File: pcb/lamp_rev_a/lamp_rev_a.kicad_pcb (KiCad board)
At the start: 4 copper layers, 100 x 80 mm, 107 parts, among them J1 TYPE-C 3.1 MT 16P, J2 DC-005-5A-2.0, J3 DB128H-5.08-2P-BK-S, Q1 AO3400A, Q2 MMBT3904, Q3 MMBT3904, Q4 MMBT3904, Q5 MMBT3904, Q6 MMBT3904, Q7 MMBT3904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

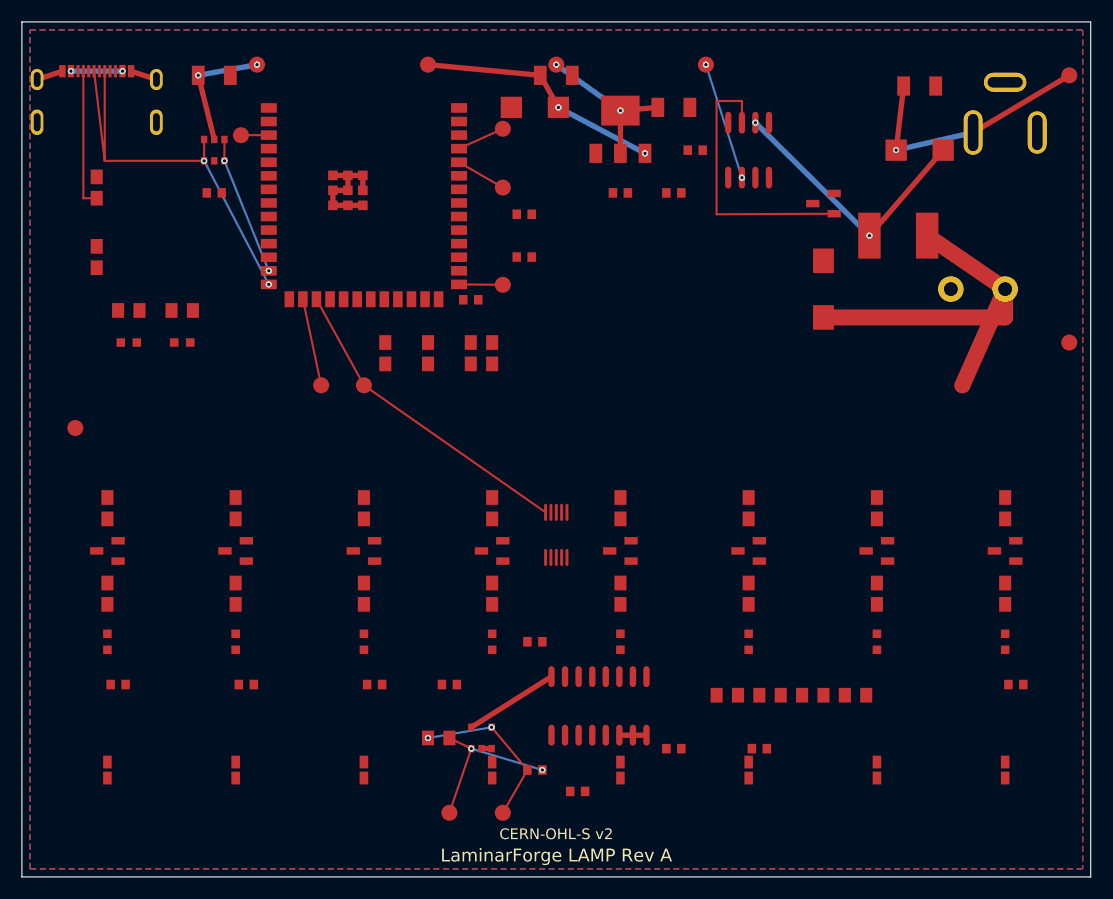
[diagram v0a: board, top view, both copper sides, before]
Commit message: Advance LAMP Rev A routed board seed
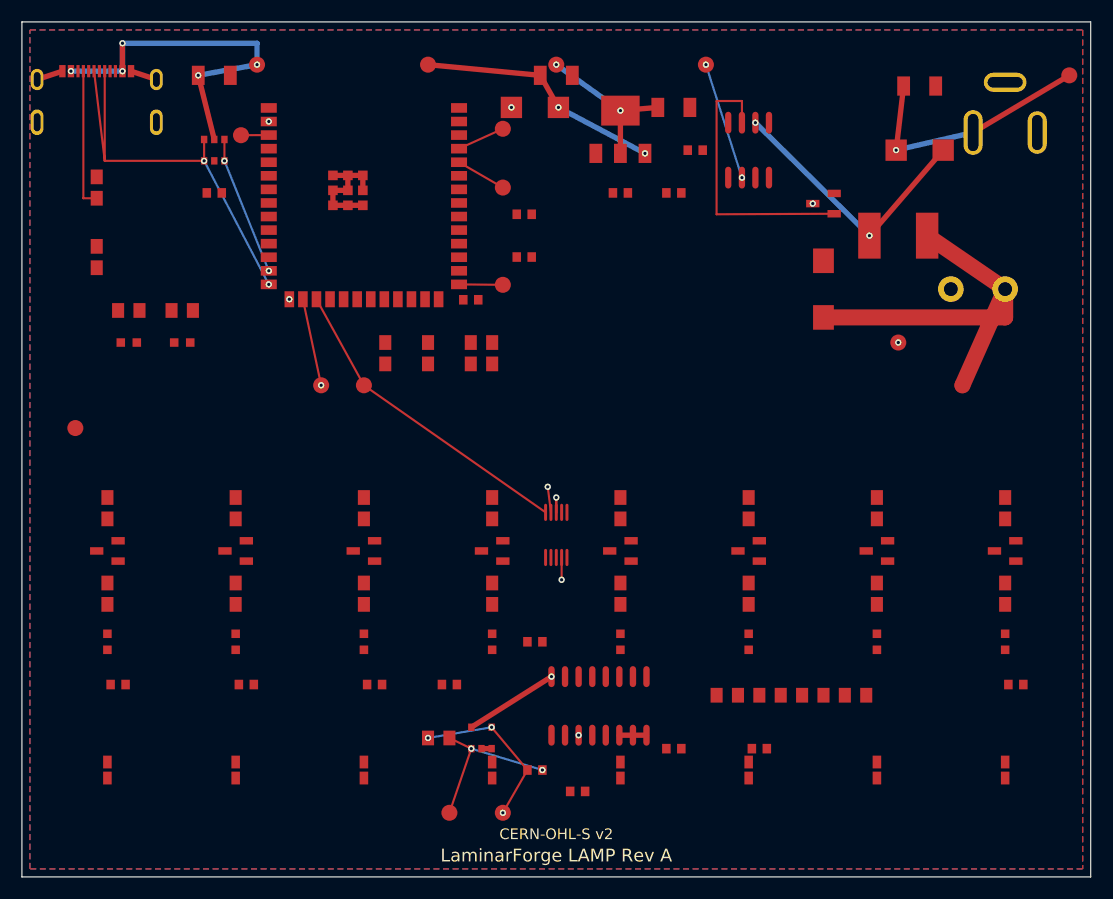
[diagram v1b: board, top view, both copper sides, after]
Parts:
- moved TP_HEATER 16.0 mm to (82.0, 30.0)
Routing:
- net +3V3: track 23.8 -> 118.4 mm, vias 2 -> 5
- net HEATER_PWM: track 11.1 -> 76.9 mm, vias 2 -> 3
- net VBUS: track 16.6 -> 60.5 mm, vias 4 -> 6
- net SDA: track 8.23 -> 41.3 mm, vias 0 -> 2
- net HEATER_P: track 0.00 -> 27.9 mm, vias 0 -> 2
- net ADC_AIN1: track 15.6 -> 41.9 mm, vias 2 -> 3
- net MUX_COM: track 15.9 -> 30.2 mm, vias 2 -> 4

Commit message: Route LAMP Rev A mux bus
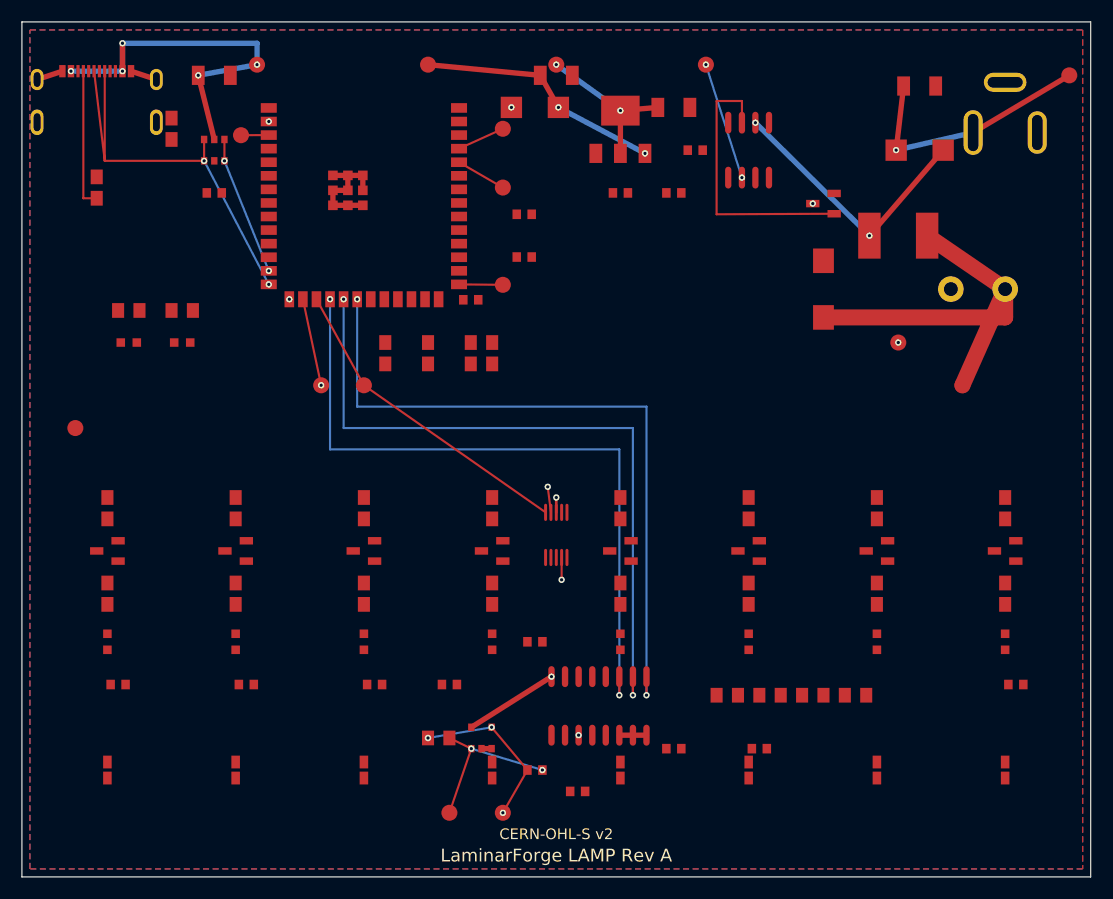
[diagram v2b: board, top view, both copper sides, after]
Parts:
- moved R2 13.9 mm to (14.0, 10.0)
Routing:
- net MUX_S2: track 0.00 -> 65.9 mm, vias 0 -> 2
- net MUX_S1: track 0.00 -> 65.9 mm, vias 0 -> 2
- net MUX_S0: track 0.00 -> 65.9 mm, vias 0 -> 2
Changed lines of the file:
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@@
   	(generator_version "10.0")
   	(layer "F.Cu")
-  	(at 7 22 90)
+  	(at 14 10 90)
   	(property "Reference" "R2"
   		(at 0 -4 0)
@@
   )
   (via
+    (at 28.830 25.950)
+    (size 0.6)
+    (drill 0.3)
+    (layers "F.Cu" "B.Cu")
+    (net 15)
+  )
+  (segment
+    (start 28.830 25.950)
+    (end 28.830 40)
+    (width 0.200)
+    (layer "B.Cu")
+    (net 15)
+  )
+  (segment
+    (start 28.830 40)
+    (end 55.900 40)
+    (width 0.200)
+    (layer "B.Cu")
+    (net 15)
+  )
+  (via
+    (at 55.900 63)
+    (size 0.6)
+    (drill 0.3)
+    (layers "F.Cu" "B.Cu")
+    (net 15)
+  )
+  (segment
+    (start 55.900 40)
+    (end 55.900 63)
+    (width 0.200)
+    (layer "B.Cu")
+    (net 15)
+  )
+  (segment
+    (start 55.900 63)
+    (end 55.900 61.260)
+    (width 0.200)
+    (layer "F.Cu")
+    (net 15)
+  )
+  (via
+    (at 30.100 25.950)
+    (size 0.6)
+    (drill 0.3)
+    (layers "F.Cu" "B.Cu")
+    (net 16)
+  )
+  (segment
+    (start 30.100 25.950)
+    (end 30.100 38)
+    (width 0.200)
+    (layer "B.Cu")
+    (net 16)
+  )
+  (segment
+    (start 30.100 38)
+    (end 57.170 38)
+    (width 0.200)
+    (layer "B.Cu")
+    (net 16)
+  )
+  (via
+    (at 57.170 63)
+    (size 0.6)
+    (drill 0.3)
+    (layers "F.Cu" "B.Cu")
+    (net 16)
+  )
+  (segment
+    (start 57.170 38)
+    (end 57.170 63)
+    (width 0.200)
+    (layer "B.Cu")
+    (net 16)
+  )
+  (segment
+    (start 57.170 63)
+    (end 57.170 61.260)
+    (width 0.200)
+    (layer "F.Cu")
+    (net 16)
+  )
+  (via
+    (at 31.370 25.950)
+    (size 0.6)
+    (drill 0.3)
+    (layers "F.Cu" "B.Cu")
+    (net 17)
+  )
+  (segment
+    (start 31.370 25.950)
+    (end 31.370 36)
+    (width 0.200)
+    (layer "B.Cu")
+    (net 17)
+  )
+  (segment
+    (start 31.370 36)
+    (end 58.440 36)
+    (width 0.200)
+    (layer "B.Cu")
+    (net 17)
+  )
+  (via
+    (at 58.440 63)
+    (size 0.6)
+    (drill 0.3)
+    (layers "F.Cu" "B.Cu")
+    (net 17)
+  )
+  (segment
+    (start 58.440 36)
+    (end 58.440 63)
+    (width 0.200)
+    (layer "B.Cu")
+    (net 17)
+  )
+  (segment
+    (start 58.440 63)
+    (end 58.440 61.260)
+    (width 0.200)
+    (layer "F.Cu")
+    (net 17)
+  )
+  (via

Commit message: Complete LAMP Rev A routed board seed
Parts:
- moved TP_EN 5.00 mm to (25.5, 10.6)
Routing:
- net USB_DN: track 13.1 -> 46.7 mm
- net USB_CC2: track 0.00 -> 21.1 mm
- net GND: track 19.7 -> 20.7 mm, vias 0 -> 2
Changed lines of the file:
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@@
   (footprint "lcsc:TESTPOINT_SMD_1.5MM"
     (layer "F.Cu")
-    (at 20.500 10.600 0)
+    (at 25.500 10.600 0)
     (property "Reference" "TP_EN" (at 0 -1.8 0) (layer "F.Fab") (effects (font (size 0.8 0.8) (thickness 0.1))))
     (property "Value" "ESP_EN" (at 0 1.8 0) (layer "F.Fab") (effects (font (size 0.8 0.8) (thickness 0.1))))
@@
   )
   (segment
-    (start 20.500 10.600)
+    (start 25.500 10.600)
     (end 23.100 10.590)
     (width 0.200)
@@
   )
   (via
+    (at 1.500 1.500)
+    (size 0.6)
+    (drill 0.3)
+    (layers "F.Cu" "B.Cu")
+    (net 1)
+  )
+  (via
+    (at 2.500 1.500)
+    (size 0.6)
+    (drill 0.3)
+    (layers "F.Cu" "B.Cu")
+    (net 1)
+  )
+  (segment
+    (start 1.500 1.500)
+    (end 2.500 1.500)
+    (width 0.500)
+    (layer "B.Cu")
+    (net 1)
+  )
+  (segment
+    (start 6.250 4.610)
+    (end 6.250 0.800)
+    (width 0.200)
+    (layer "F.Cu")
+    (net 19)
+  )
+  (segment
+    (start 7.250 4.610)
+    (end 7.250 0.800)
+    (width 0.200)
+    (layer "F.Cu")
+    (net 19)
+  )
+  (segment
+    (start 6.250 0.800)
+    (end 7.250 0.800)
+    (width 0.200)
+    (layer "F.Cu")
+    (net 19)
+  )
+  (segment
+    (start 7.250 0.800)
+    (end 20.500 0.800)
+    (width 0.200)
+    (layer "F.Cu")
+    (net 19)
+  )
+  (segment
+    (start 20.500 0.800)
+    (end 20.500 11)
+    (width 0.200)
+    (layer "F.Cu")
+    (net 19)
+  )
+  (segment
+    (start 20.500 11)
+    (end 18.950 11)
+    (width 0.200)
+    (layer "F.Cu")
+    (net 19)
+  )
+  (segment
+    (start 8.750 4.610)
+    (end 8.750 1.400)
+    (width 0.200)
+    (layer "F.Cu")
+    (net 21)
+  )
+  (segment
+    (start 8.750 1.400)
+    (end 15.500 1.400)
+    (width 0.200)
+    (layer "F.Cu")
+    (net 21)
+  )
+  (segment
+    (start 15.500 1.400)
+    (end 15.500 11)
+    (width 0.200)
+    (layer "F.Cu")
+    (net 21)
+  )
+  (segment
+    (start 15.500 11)
+    (end 14 11)
+    (width 0.200)
+    (layer "F.Cu")
+    (net 21)
+  )
+  (via
     (at 28.830 25.950)
     (size 0.6)
@@
     (connect_pads yes (clearance 0.200))
     (min_thickness 0.150)
-    (fill yes (thermal_gap 0.300) (thermal_bridge_width 0.300))
+    (fill yes (thermal_gap 0.300) (thermal_bridge_width 0.300) (island_removal_mode 0))
     (polygon
       (pts
@@
     (connect_pads yes (clearance 0.200))
     (min_thickness 0.150)
-    (fill yes (thermal_gap 0.300) (thermal_bridge_width 0.300))
+    (fill yes (thermal_gap 0.300) (thermal_bridge_width 0.300) (island_removal_mode 0))
     (polygon
       (pts

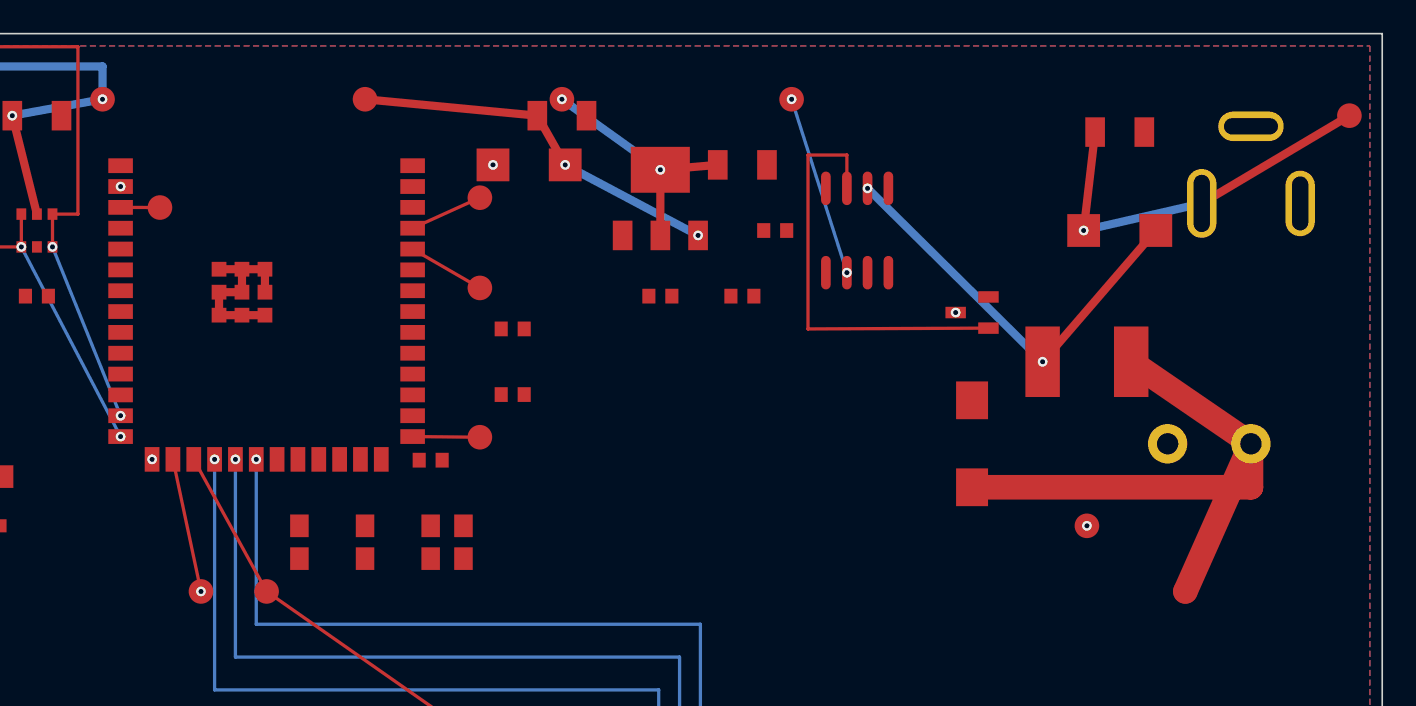
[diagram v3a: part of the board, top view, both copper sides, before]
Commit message: Add LAMP Rev A electrical validation gate
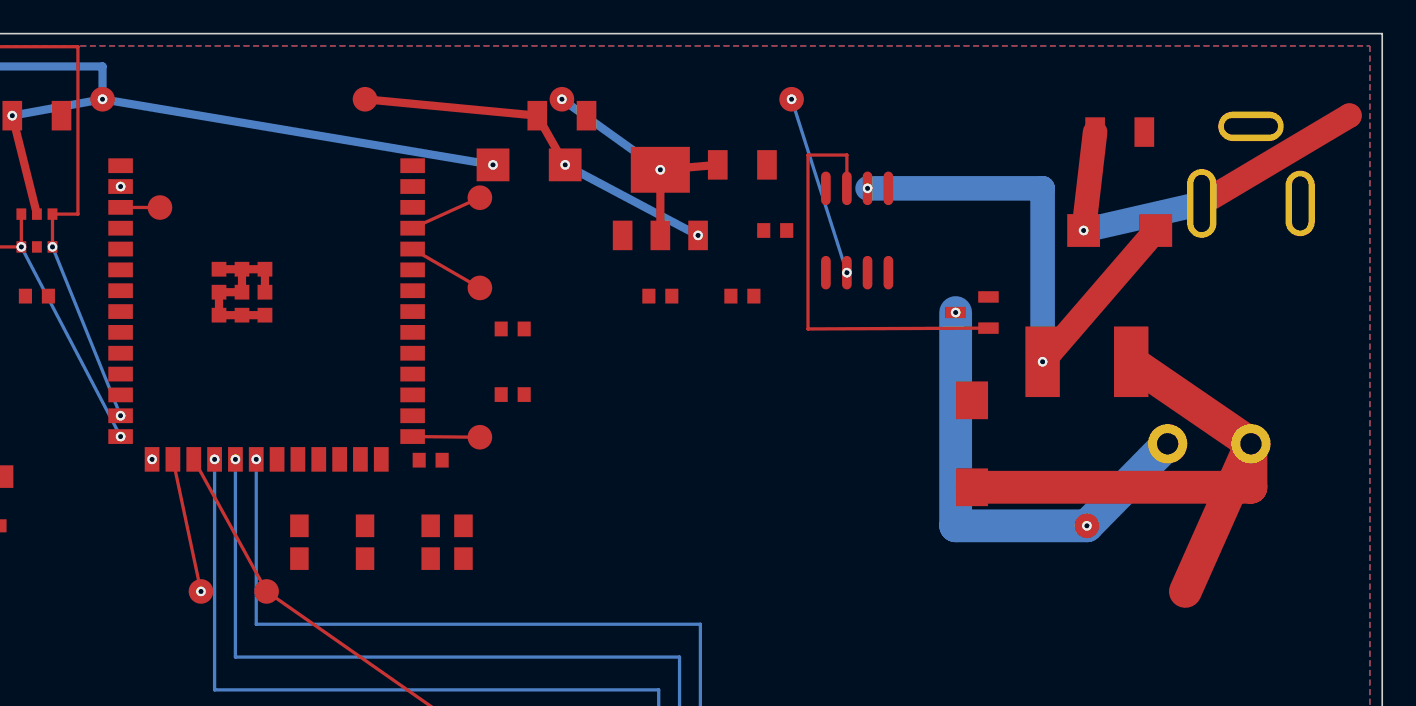
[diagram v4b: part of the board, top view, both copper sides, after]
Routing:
- net +12V: track 25.6 -> 31.8 mm
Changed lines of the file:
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@@
     (start 82.500 6)
     (end 81.800 12)
-    (width 0.500)
+    (width 1.500)
     (layer "F.Cu")
     (net 2)
@@
     (start 81.800 12)
     (end 89 10.350)
-    (width 0.500)
+    (width 1.500)
     (layer "B.Cu")
     (net 2)
@@
     (start 92 25)
     (end 84.700 20)
-    (width 1.500)
+    (width 2)
     (layer "F.Cu")
     (net 7)
@@
     (start 88 34)
     (end 92 25)
-    (width 1.500)
+    (width 2)
     (layer "F.Cu")
     (net 7)
@@
     (start 79.300 20)
     (end 86.200 12)
-    (width 0.500)
+    (width 1.500)
     (layer "F.Cu")
     (net 3)
@@
     (start 89 10.350)
     (end 98 5)
-    (width 0.500)
+    (width 1.500)
     (layer "F.Cu")
     (net 2)
@@
     (net 3)
   )
+  (segment
+    (start 68.630 9.430)
+    (end 79.300 9.430)
+    (width 1.500)
+    (layer "B.Cu")
+    (net 3)
+  )
   (via
     (at 79.300 20)
@@
   )
   (segment
-    (start 68.630 9.430)
+    (start 79.300 9.430)
     (end 79.300 20)
-    (width 0.500)
+    (width 1.500)
     (layer "B.Cu")
     (net 3)
@@
     (start 92 25)
     (end 92 27.650)
-    (width 1.500)
+    (width 2)
     (layer "F.Cu")
     (net 7)
@@
     (start 92 27.650)
     (end 75 27.650)
-    (width 1.500)
+    (width 2)
     (layer "F.Cu")
     (net 7)
@@
     (end 22 4)
     (width 0.500)
-    (layer "In2.Cu")
+    (layer "B.Cu")
     (net 22)
   )
@@
   (segment
     (start 74 17)
-    (end 86.920 17)
-    (width 1.500)
-    (layer "In2.Cu")
+    (end 74 30)
+    (width 2)
+    (layer "B.Cu")
     (net 6)
   )
-  (segment
-    (start 86.920 17)
-    (end 86.920 25)
-    (width 1.500)
-    (layer "In2.Cu")
+  (via
+    (at 82 30)
+    (size 0.6)
+    (drill 0.3)
+    (layers "F.Cu" "B.Cu")
+    (net 6)
+  )
+  (segment
+    (start 74 30)
+    (end 82 30)
+    (width 2)
+    (layer "B.Cu")
     (net 6)
   )
@@
   )
   (segment
+    (start 22 4)
+    (end 22 4.300)
+    (width 0.500)
+    (layer "F.Cu")
+    (net 22)
+  )
+  (segment
     (start 55.900 63)
     (end 55.900 61.260)
@@
     (net 11)
   )
-  (via
-    (at 82 30)
-    (size 0.6)
-    (drill 0.3)
-    (layers "F.Cu" "B.Cu")
+  (segment
+    (start 82 30)
+    (end 86.920 25)
+    (width 2)
+    (layer "B.Cu")
     (net 6)
   )
-  (segment
-    (start 86.920 25)
-    (end 82 30)
-    (width 1.500)
-    (layer "In2.Cu")
-    (net 6)
-  )
